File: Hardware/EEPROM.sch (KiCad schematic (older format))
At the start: 7 parts, among them J3 Jumper, U1 EEPROM

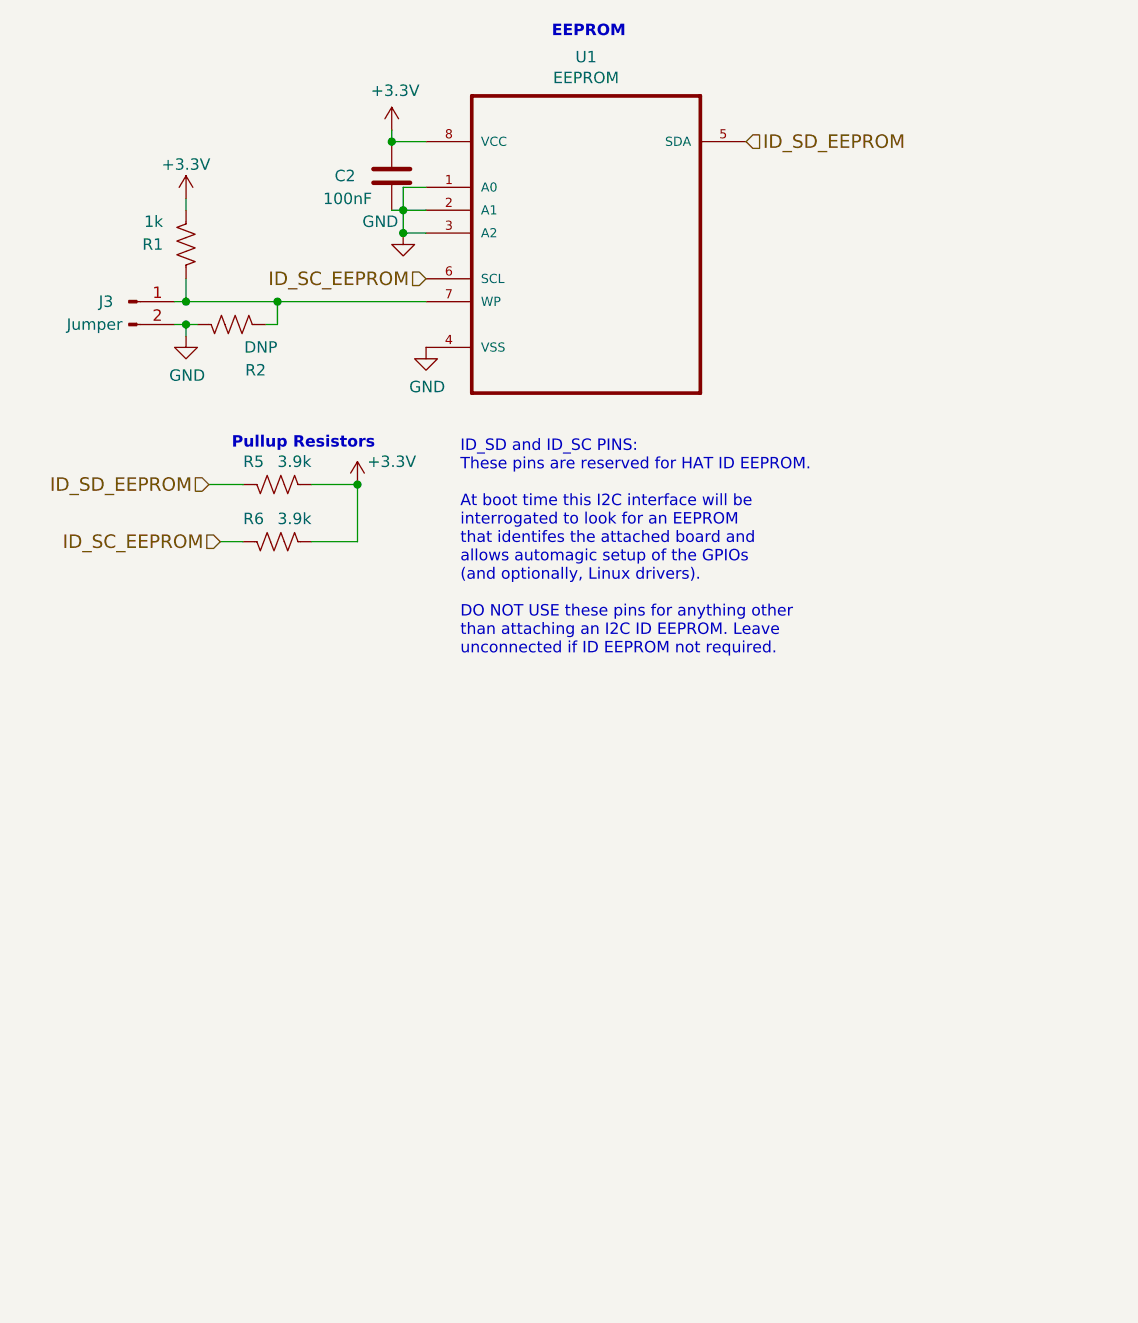
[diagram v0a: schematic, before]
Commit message: Up Changed I2C addres for DAC and ADC.  Added MOSFET to USART RX.
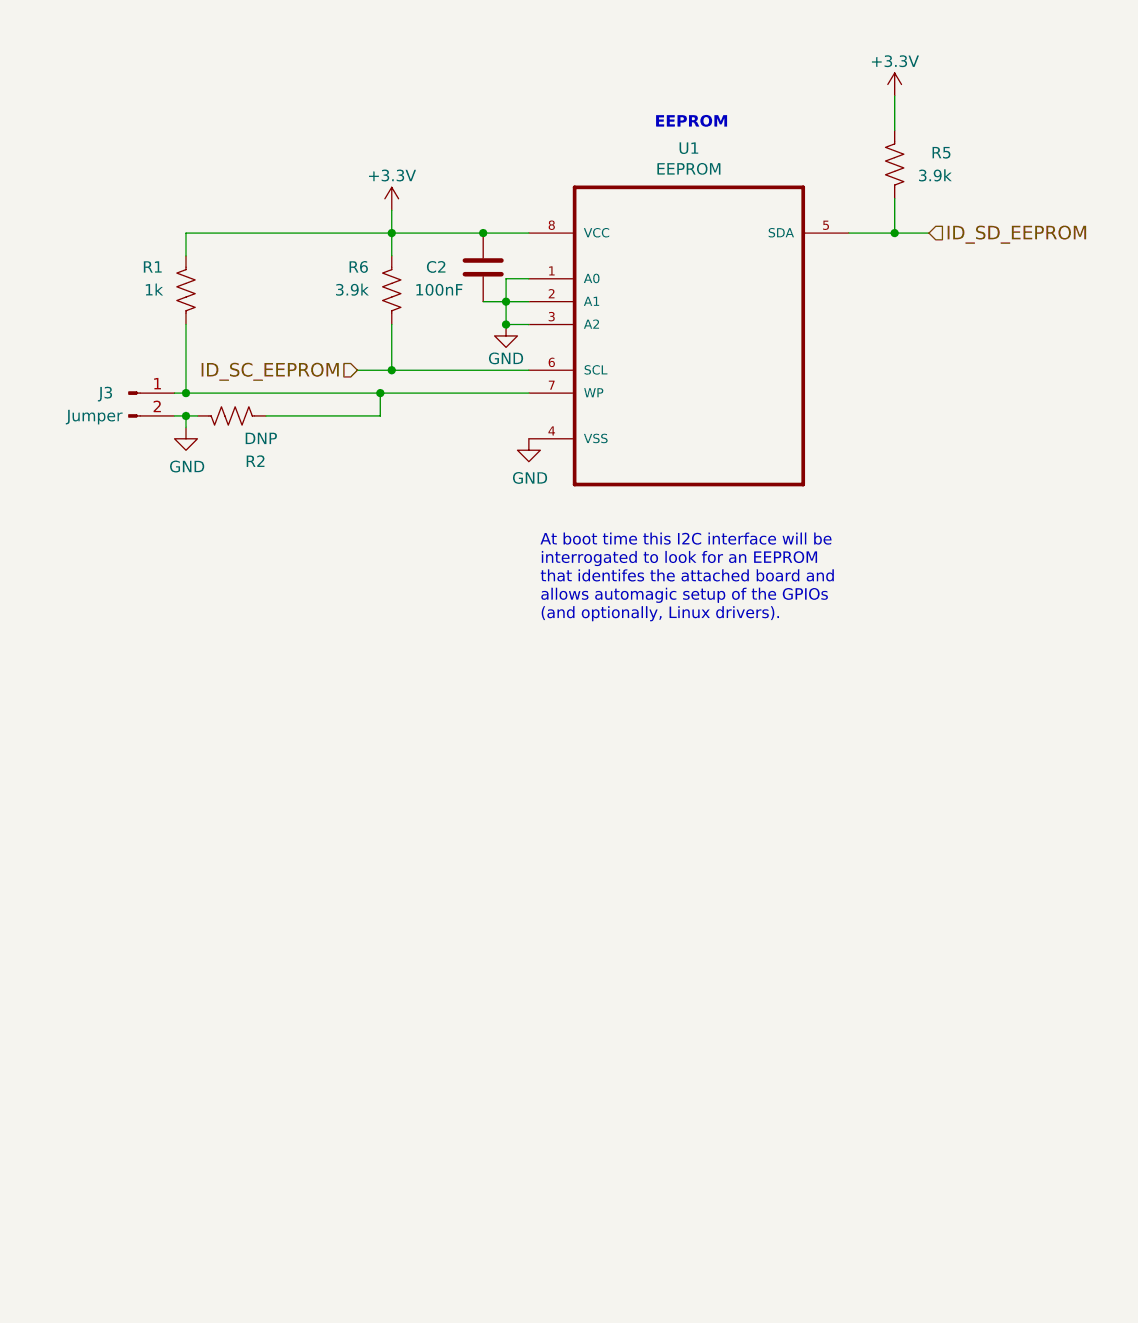
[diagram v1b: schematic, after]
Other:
- note added: "At boot time this I2C interface will be\ninterrogated to look for an EEPROM\nthat identifes the attached board and\nallows automagic setup of the GPIOs\n(and optionally, Linux drivers)."
- note removed: "ID_SD and ID_SC PINS:\nThese pins are reserved for HAT ID EEPROM.\n\nAt boot time this I2C interface will be\ninterrogated to look for an EEPROM\nthat identifes the attached board and\nallows automagic setup of the GPIOs\n(and optionally, Linux drivers).\n\nDO NOT USE these pins for anything other\nthan attaching an I2C ID EEPROM. Leave\nunconnected if ID EEPROM not required."
- note removed: "Pullup Resistors"
- moved on the sheet: C2, J3, R1, R2, R5, R6, U1

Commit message: Updated Schematic Attribution and Documentation
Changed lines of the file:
@@
 EESchema Schematic File Version 4
+LIBS:Zephyrus-IAQ-HAT-cache
 EELAYER 30 0
 EELAYER END
-$Descr A4 11693 8268
+$Descr USLetter 11000 8500
 encoding utf-8
-Sheet 4 7
+Sheet 7 7
 Title "Raspberry Pi HAT Specifications"
 Date "2019-11-15"
@@
 	7000 3450 7150 3450
 Connection ~ 7000 3450
+$Comp
+L cc-by-sa:LOGO #G?
+U 1 1 5DD4FDD6
+P 5350 7550
+AR Path="/5DB861AF/5DD4FDD6" Ref="#G?"  Part="1"
+AR Path="/5DAFB35B/5DD4FDD6" Ref="#G7"  Part="1"
+F 0 "#G7" H 5350 7287 60  0001 C CNN
+F 1 "LOGO" H 5350 7813 60  0001 C CNN
+F 2 "" H 5350 7550 50  0001 C CNN
+F 3 "" H 5350 7550 50  0001 C CNN
+	1    5350 7550
+	1    0    0    -1
+$EndComp
 $EndSCHEMATC
